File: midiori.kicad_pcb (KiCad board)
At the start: 2 copper layers, 141 x 150 mm, 86 parts, among them J1 midiori-rescue_x68000_expansi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, J2 Conn_ARM_JTAG_SWD_10, J3 AudioJack3, J4 Mini-DIN-5, J5 AudioJack3, J6 AudioJack3, J7 Conn_01x06, J8 AudioJack3, J9 Mini-DIN-5, U1 74LCX07, U10 ICE40HX1K-TQ144, U11 AP2205K-3.3, U12 AK4432, U13 TL074, U14 AP2205K-3.3, U15 TL072, U16 74LCX07, U17 H11L1, U18 SN74LVC245APW, U2 AT25SF081-SSHD-X, U3 AP2127K-1.2, U4 SN74LVC245APW, U5 SN74LVC245APW, U6 SN74LVC245APW, U7 SN74LVC245APW, U8 SN74LVC245APW, U9 SN74LVC245APW, X1 16MHz, X2 24.576MHz

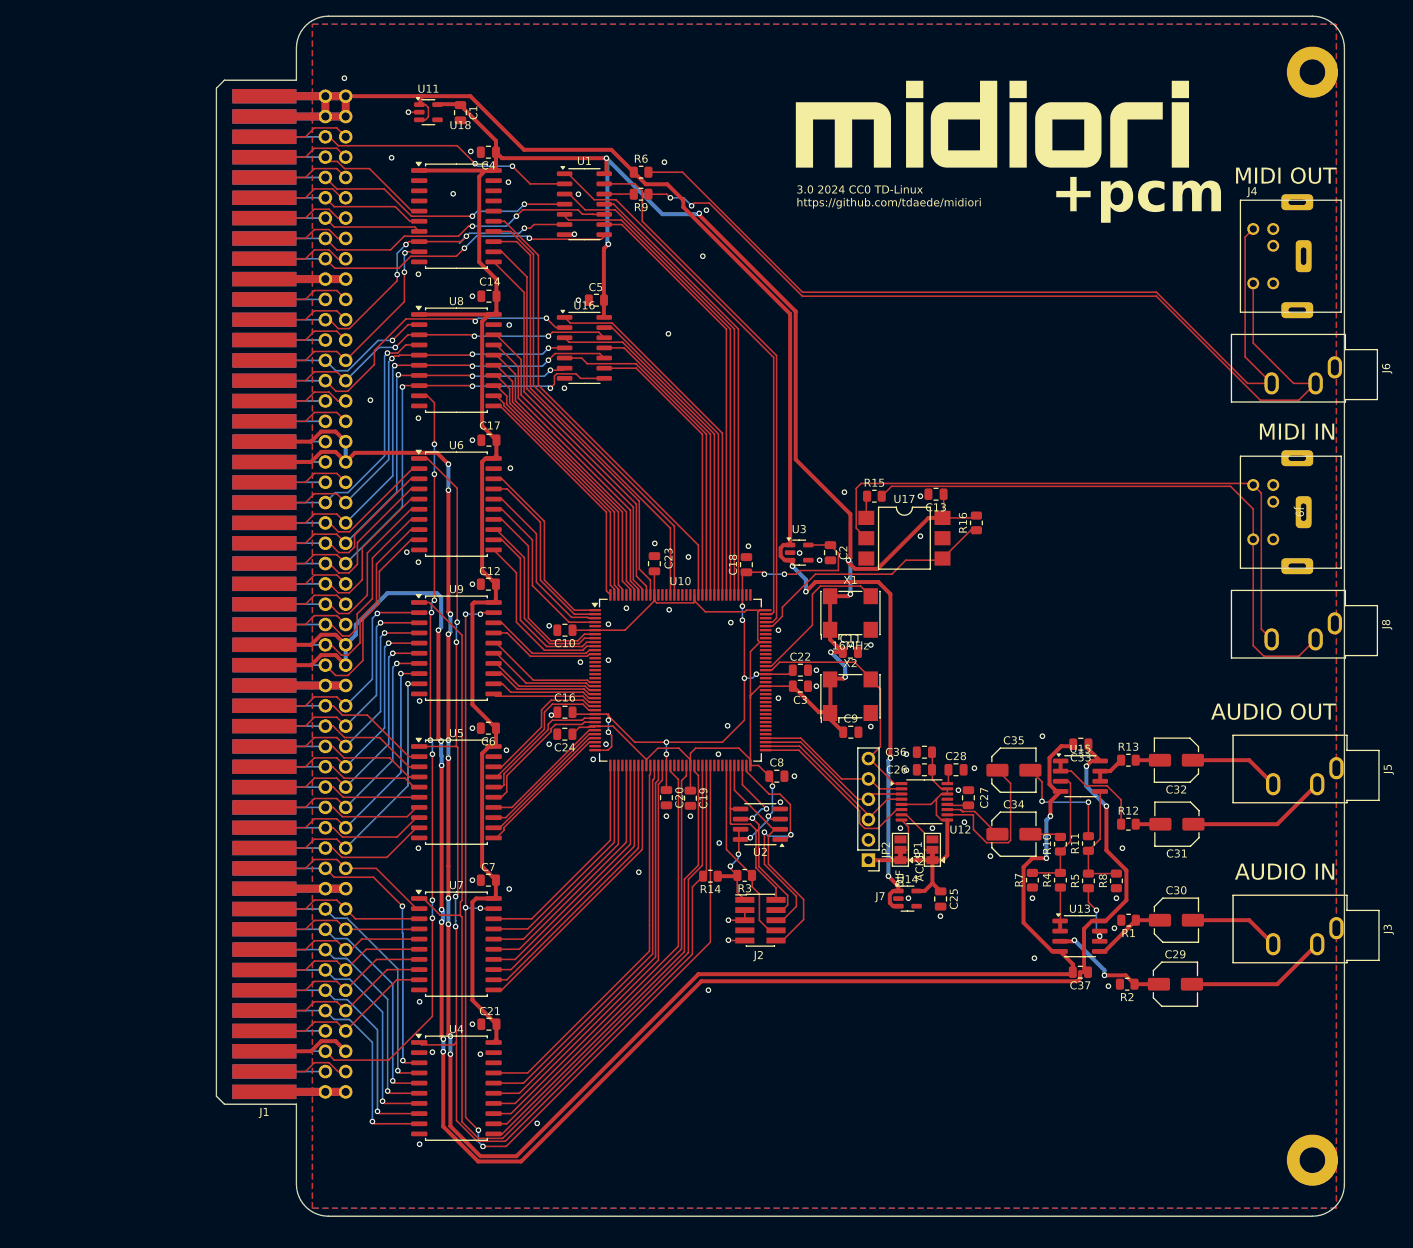
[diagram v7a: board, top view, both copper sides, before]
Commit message: some extra test pads
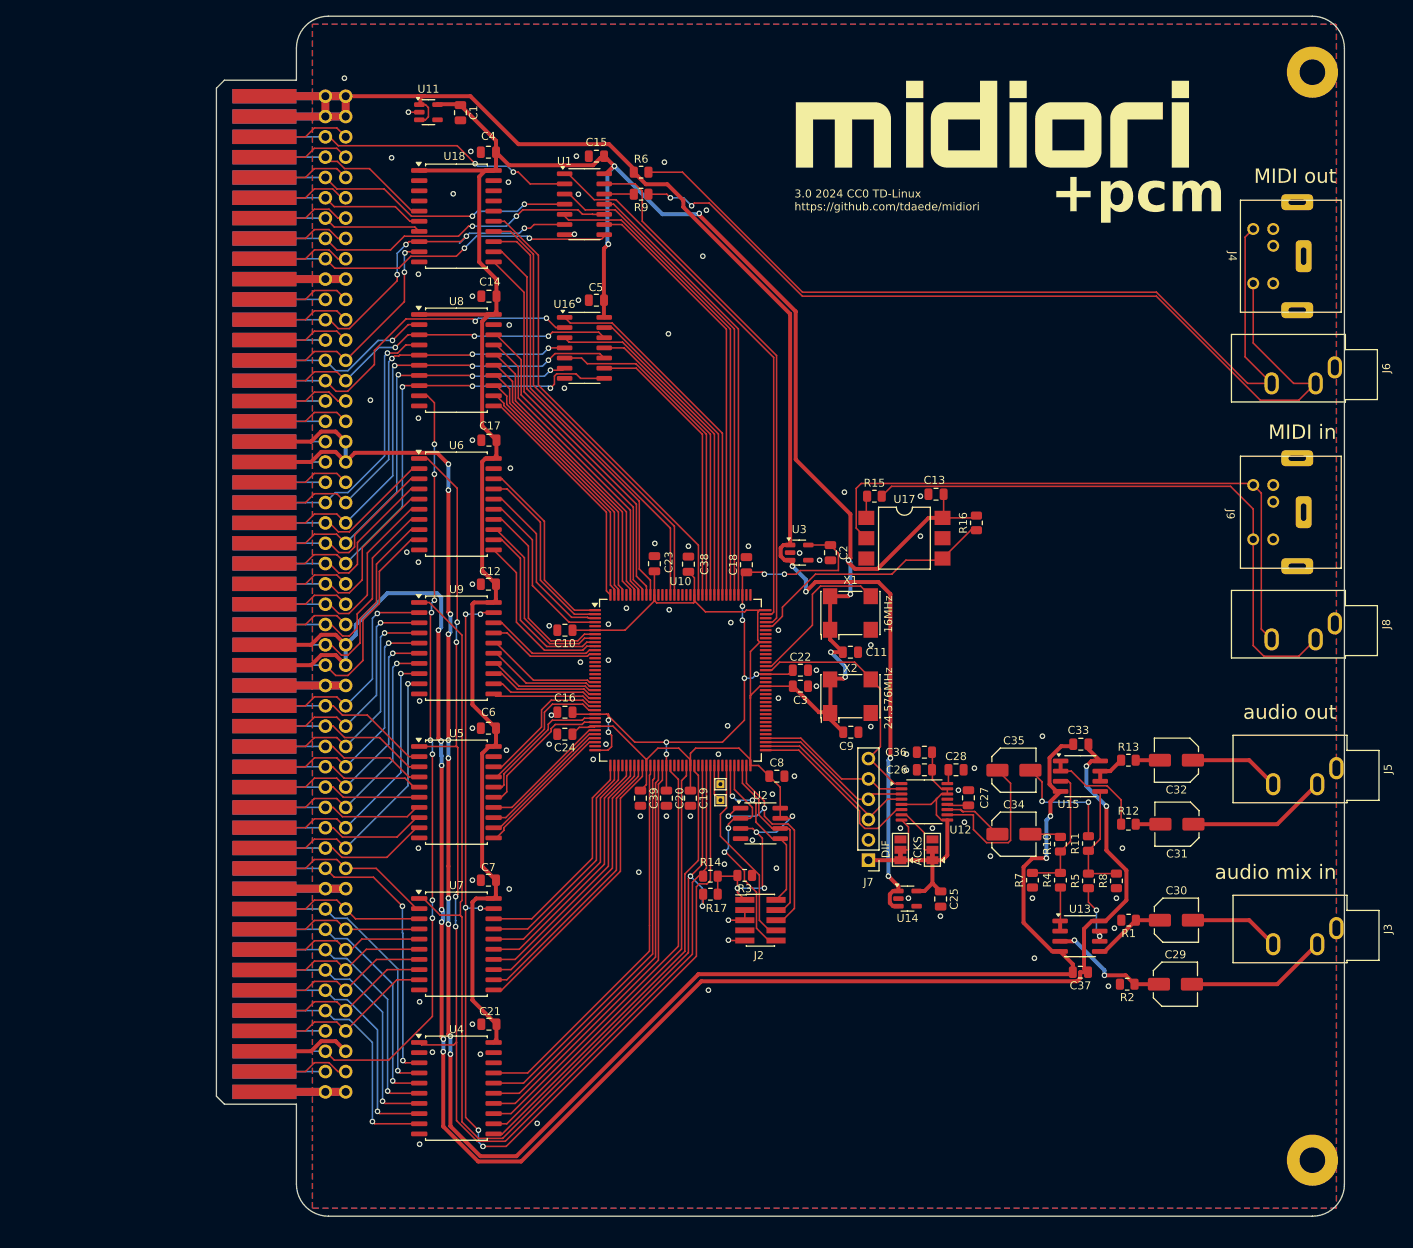
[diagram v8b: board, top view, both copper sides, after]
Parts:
- added C15: 0.1uF, Capacitor_SMD:C_0805_2012Metric, F.Cu at (91.5, 56.5)
- added C38: 0.1uF, Capacitor_SMD:C_0805_2012Metric, F.Cu at (103.0, 107.5)
- added C39: 0.1uF, Capacitor_SMD:C_0805_2012Metric, F.Cu at (97.0, 136.8)
- added R17: 10k, Resistor_SMD:R_0805_2012Metric, F.Cu at (105.8, 148.8)
- added TP1: TestPoint, TestPoint:TestPoint_THTPad_1.0x1.0mm_Drill0.5mm, F.Cu at (107.0, 137.0)
- added TP2: TestPoint, TestPoint:TestPoint_THTPad_1.0x1.0mm_Drill0.5mm, F.Cu at (107.0, 135.0)
- moved U2 0.10 mm to (112.0, 139.9), turned to 0 degrees
- moved C20 0.06 mm to (100.2, 136.8)
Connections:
- U10 pad 63: unconnected-(U10C-IOB_42_CBSEL0-Pad63) -> /CBSEL0
- U10 pad 64: unconnected-(U10C-IOB_43_CBSEL1-Pad64) -> /CBSEL1
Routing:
- net +3V3: track 437.4 -> 453.2 mm, vias 12 -> 11
- net /data_dir: track 137.0 -> 142.9 mm, vias 0 -> 2
- net /CBSEL0: track 0.00 -> 4.66 mm
- net /CBSEL1: track 0.00 -> 2.44 mm
- net /sck: track 25.1 -> 22.9 mm, vias 2 -> 0
- net /so: track 29.9 -> 28.7 mm, vias 0 -> 2
- net /reset: track 23.7 -> 24.3 mm
- net /si: track 21.9 -> 22.5 mm, vias 0 -> 2
- net /xltr_oe: track 135.6 -> 136.2 mm
- net GND: track 99.3 -> 99.6 mm, vias 89 -> 93
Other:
- board text added: "24.576MHz"
- board text added: "MIDI in"
- board text added: "MIDI out"
- board text added: "audio mix in"
- board text added: "audio out"
- board text removed: "AUDIO IN"
- board text removed: "AUDIO OUT"
- board text removed: "MIDI IN"
- board text removed: "MIDI OUT"
